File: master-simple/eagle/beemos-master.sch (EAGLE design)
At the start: 62 parts, among them CON1 BAT, CON2 JACK_DC_BARREL, CON3 SPI, IC1 32U4, IC2 MCP73831T, IC3 MCP1703CB, IC4 DMP1045U, IC5 MS5637WIDE, J1 RJ123.3, J10 RJ12STRAIGHT-I2C, J2 RJ123.3, J3 RJ123.3, J4 RJ123.3, J5 RJ123.3, J6 RJ123.3, J8 RJ123.3, J9 RJ12STRAIGHT-I2C, X1 8MHz, X2 MINI-USB, X3 1503_09

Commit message: Reorganized components, placement. Cleanup of temporary files
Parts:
- removed 100K: 100k, rcl:R-EU_R0805
- removed 868MHZ: (no value), sma_end_launch:SMACONNECTOR_EDGE_UFL
- removed C12, C13: 100n, rcl:C-EUC0805
- removed IC5: MS5637WIDE, MS5637:MS5637WIDE
- removed J10, J9: RJ12STRAIGHT-I2C, lpatiny:RJ12STRAIGHT-I2C
- removed J5, J6, J8: RJ123.3, lpatiny:RJ123.3
- removed SJ4, SJ5: JUMPER-PAD-2-NC_BY_TRACE, SparkFun-Passives:JUMPER-PAD-2-NC_BY_TRACE
- removed U$7: RN2483_SIMPLE, Octanis1_bioreactorPort:RN2483_SIMPLE
- added R13: 100, rcl:R-EU_R0805
- added R7: 1K, rcl:R-EU_R0805
- added R8, RT3: 4.7k, resistor:R-EU_R0805
- added U2: (no value), RHT03_DHT-22_AM2302:RHT03_DHT-22_AM2302
- added X4: 1503_09, con-lumberg:1503_09
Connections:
- removed net ANGND: 868MHZ.GND1, 868MHZ.GND2, 868MHZ.GND3, 868MHZ.GND4, C12.2, C13.2, SJ4.2, SJ5.2, U$7.P$1, U$7.P$21, U$7.P$26, U$7.P$27, U$7.P$33
- removed net ANT868: 868MHZ.ANT, U$7.P$23
- removed net N$27: J8.1
- removed net N$28: J8.2
- removed net N$29: J8.3
- removed net N$30: J8.4
- removed net N$31: J8.5
- removed net N$32: J8.6
- removed net N$33: J9.1
- removed net N$36: J9.4
- removed net N$37: J9.5
- removed net N$40: J9.6
- removed net N$44: J10.1
- removed net N$47: J10.4
- removed net N$48: J10.5
- removed net N$49: J10.6
- new net A8: R7.1
- new net N$2: R7.2, RT3.2, X4.2
- new net N$4: R13.1, RT3.1, X4.1
- net 3.3V: now also R13.2; no longer 100K.1, C12.1, C13.1, J5.5, J6.5, U$7.P$12
- net A2: no longer 100K.2, U$7.P$32
- net A4: no longer J5.3
- net D11: no longer J5.2
- net D12: no longer J6.3
- net D6: now also R8.1, U2.DATA; no longer J2.2
- net D7: now also R8.2, U2.VDD
- net D8: now also J2.2; no longer J6.2
- net GND: now also U2.GND, X4.3; no longer J5.4, J6.4, SJ4.1, SJ5.1
- net RX: no longer U$7.P$6
- net SCL: no longer J10.2, J5.1, J6.1, J9.2
- net SDA: no longer J10.3, J5.6, J6.6, J9.3
- net TX: no longer U$7.P$7
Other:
- note added: "I2C"
- note removed: "Barometric pressure"
- note removed: "LoRa RN2483"
- note removed: "RJ12 connectors"
- moved on the sheet: J1, J2, J3, J4, R10, R2, R9, RT1, RT2, X3

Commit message: Almost finished beemos master board (labels to do still)
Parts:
- removed U$6: SIM800L, SIM800L:SIM800L
- removed U$8: DS18B20, lpatiny:DS18B20SMALL
- removed U2: (no value), RHT03_DHT-22_AM2302:RHT03_DHT-22_AM2302
- added JP1: (no value), SparkFun:M06RA
- added R14, R16: 10k, rcl:R-EU_R0805
- added X5: 1503_09, con-lumberg:1503_09
- J1, J2, J3, J4: value RJ123.3 -> RJ12STRAIGHT-I2C; device lpatiny:RJ123.3 -> lpatiny:RJ12STRAIGHT-I2C
- R10: value 1K -> 100
- R8: value 4.7k -> 1K; device resistor:R-EU_R0805 -> rcl:R-EU_R0805
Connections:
- removed net A7: R9.1
- removed net A8: R7.1
- removed net D12*: R10.1
- removed net D14: R1.2, R6.2, U$1.VCC
- removed net N$15: C5.1, D1.C, D2.C, D3.A, D4.C, IC2.VDD, IC4.G, R15.2
- new net N$5: C5.1, D1.C, D2.C, D3.A, D4.C, IC2.VDD, IC4.G, R14.1, R15.2
- new net N$7: R16.2
- new net N$8: R8.2, RT2.2, X5.2
- net 3.3V: now also R10.2; no longer J1.5, J2.5, J3.5, J4.5, RT2.1, U$6.RST, U$8.VDD
- net A0: no longer J1.3
- net A1: no longer J2.3
- net A2: no longer J3.3
- net A3: no longer J4.3
- net A5: now also R14.2, R16.1
- net D10: now also R9.1; no longer J4.2
- net D11: now also R7.1
- net D5: no longer J1.2
- net D6: now also JP1.3; no longer R8.1, U2.DATA
- net D7: now also R8.1; no longer R8.2, U2.VDD
- net D8: no longer J2.2
- net D9: now also U$1.VCC; no longer J3.2
- net GND: now also J1.6, J2.6, J3.6, J4.6, JP1.6, X5.3; no longer U$6.GND, U$8.GND, U2.GND
- net N$9: now also R10.1, RT2.1, X5.1; no longer R10.2, RT2.2, U$8.DQ
- net RX: now also JP1.5; no longer U$6.TXD
- net SCL: now also J1.2, J2.2, J3.2, J4.2; no longer J1.1, J2.1, J3.1, J4.1
- net SDA: now also J1.3, J2.3, J3.3, J4.3; no longer J1.6, J2.6, J3.6, J4.6
- net TX: now also JP1.4; no longer U$6.RXD
- net VBAT1: now also JP1.2; no longer U$6.VDD
- net VDD: now also J1.5, J2.5, J3.5, J4.5, R1.2, R6.2
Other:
- moved on the sheet: J1, J2, J3, J4, R10, R13, R7, R8, RT2, RT3, X4

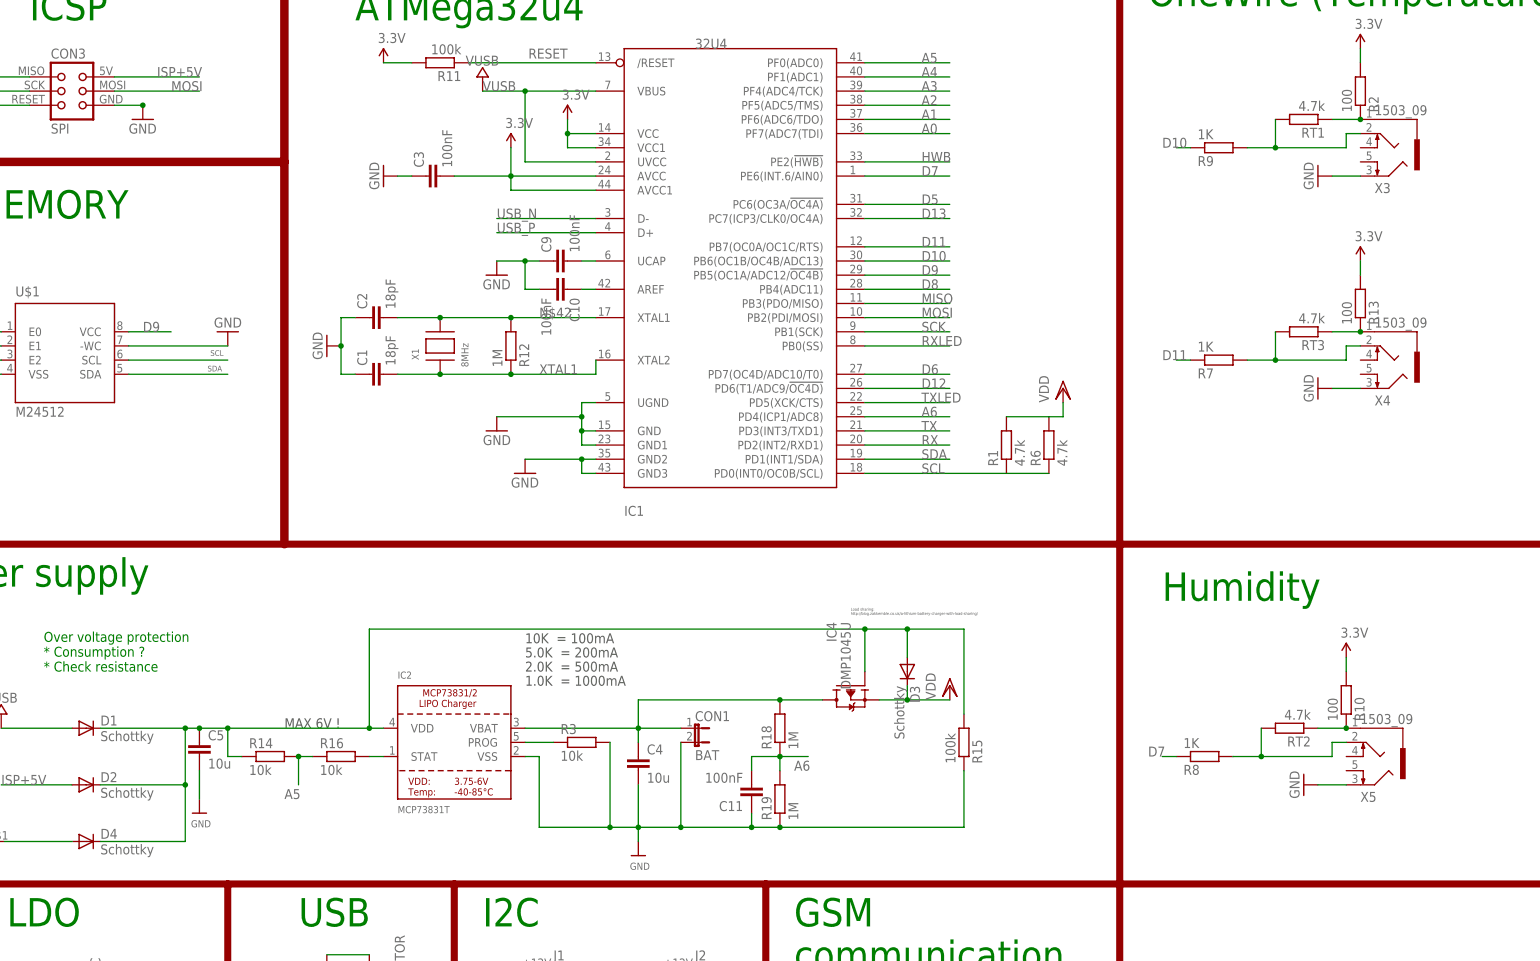
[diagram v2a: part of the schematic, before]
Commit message: Repositioned labels on the board layout
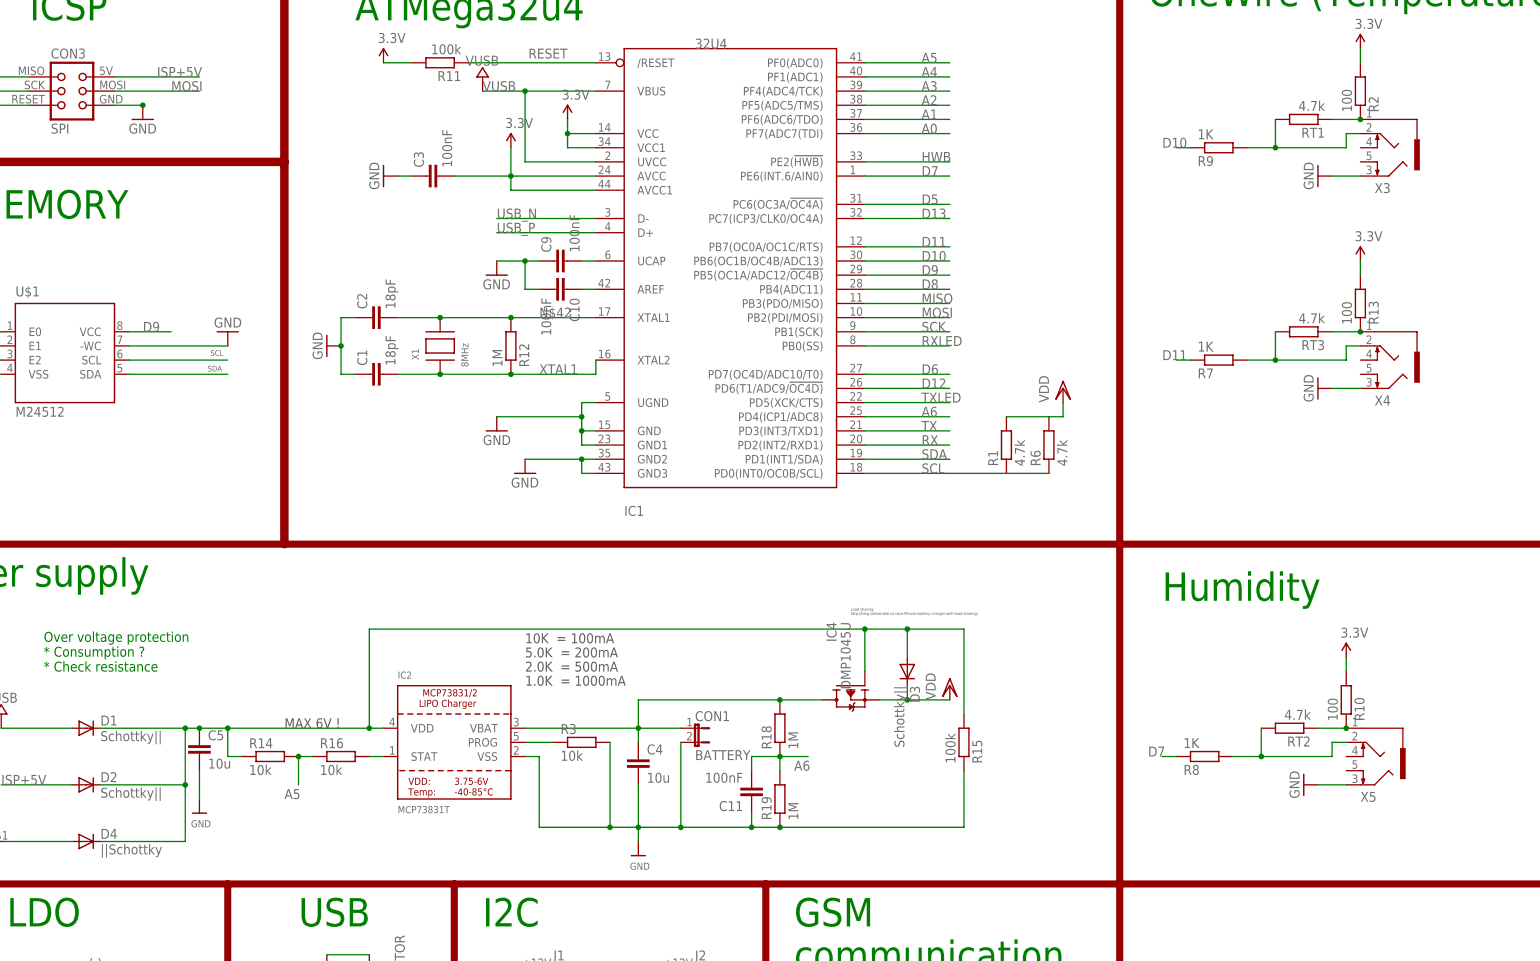
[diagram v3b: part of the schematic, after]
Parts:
- CON1: value BAT -> BATTERY
- D1, D2, D3: value Schottky -> Schottky||
- D4: value Schottky -> ||Schottky
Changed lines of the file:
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@@
 <?xml version="1.0" encoding="utf-8"?>
 <!DOCTYPE eagle SYSTEM "eagle.dtd">
-<eagle version="8.7.1">
+<eagle version="9.0.0">
 <drawing>
 <settings>
@@
 <attribute name="MPN" value="RC1206FR-07100KL"/>
 </part>
-<part name="D3" library="diode" library_urn="urn:adsk.eagle:library:210" deviceset="MBR0520LT" device="" package3d_urn="urn:adsk.eagle:package:43420/1" value="Schottky">
+<part name="D3" library="diode" library_urn="urn:adsk.eagle:library:210" deviceset="MBR0520LT" device="" package3d_urn="urn:adsk.eagle:package:43420/1" value="Schottky||">
 <attribute name="LCSC" value="C82544"/>
 <attribute name="MPN" value="621-1N5819HW-F"/>
@@
 <part name="SUPPLY4" library="supply1" library_urn="urn:adsk.eagle:library:371" deviceset="VDD" device=""/>
 <part name="U$2" library="MyPOW" deviceset="VUSB" device=""/>
-<part name="D1" library="diode" library_urn="urn:adsk.eagle:library:210" deviceset="MBR0520LT" device="" package3d_urn="urn:adsk.eagle:package:43420/1" value="Schottky">
+<part name="D1" library="diode" library_urn="urn:adsk.eagle:library:210" deviceset="MBR0520LT" device="" package3d_urn="urn:adsk.eagle:package:43420/1" value="Schottky||">
 <attribute name="LCSC" value="C82544"/>
 <attribute name="MPN" value="621-1N5819HW-F"/>
 </part>
-<part name="D2" library="diode" library_urn="urn:adsk.eagle:library:210" deviceset="MBR0520LT" device="" package3d_urn="urn:adsk.eagle:package:43420/1" value="Schottky">
+<part name="D2" library="diode" library_urn="urn:adsk.eagle:library:210" deviceset="MBR0520LT" device="" package3d_urn="urn:adsk.eagle:package:43420/1" value="Schottky||">
 <attribute name="LCSC" value="C82544"/>
 <attribute name="MPN" value="621-1N5819HW-F"/>
@@
 <attribute name="MPN" value="RC1206FR-07100KL"/>
 </part>
-<part name="CON1" library="jumper" library_urn="urn:adsk.eagle:library:252" deviceset="JP1E" device="" package3d_urn="urn:adsk.eagle:package:15455/1" value="BAT"/>
+<part name="CON1" library="jumper" library_urn="urn:adsk.eagle:library:252" deviceset="JP1E" device="" package3d_urn="urn:adsk.eagle:package:15455/1" value="BATTERY"/>
 <part name="R18" library="rcl" deviceset="R-EU_" device="R0805" value="1M">
 <attribute name="ELECROW" value="C17514"/>
@@
 <part name="J4" library="lpatiny" deviceset="RJ12" device="STRAIGHT-I2C" value="RJ12STRAIGHT-I2C"/>
 <part name="CON2" library="lpatiny" deviceset="JACK_DC_BARREL" device=""/>
-<part name="D4" library="diode" library_urn="urn:adsk.eagle:library:210" deviceset="MBR0520LT" device="" package3d_urn="urn:adsk.eagle:package:43420/1" value="Schottky">
+<part name="D4" library="diode" library_urn="urn:adsk.eagle:library:210" deviceset="MBR0520LT" device="" package3d_urn="urn:adsk.eagle:package:43420/1" value="||Schottky">
 <attribute name="LCSC" value="C82544"/>
 <attribute name="MPN" value="621-1N5819HW-F"/>
@@
 <part name="R9" library="rcl" deviceset="R-EU_" device="R0805" value="1K"/>
 <part name="P+37" library="SparkFun" deviceset="3.3V" device=""/>
-<part name="X3" library="con-lumberg" deviceset="1503_09" device=""/>
+<part name="X3" library="con-lumberg" deviceset="1503_09" device="" value=""/>
 <part name="R2" library="rcl" deviceset="R-EU_" device="R0805" value="100"/>
 <part name="GND1" library="supply1" deviceset="GND" device=""/>
@@
 <part name="R7" library="rcl" deviceset="R-EU_" device="R0805" value="1K"/>
 <part name="P+5" library="SparkFun" deviceset="3.3V" device=""/>
-<part name="X4" library="con-lumberg" deviceset="1503_09" device=""/>
+<part name="X4" library="con-lumberg" deviceset="1503_09" device="" value=""/>
 <part name="R13" library="rcl" deviceset="R-EU_" device="R0805" value="100"/>
 <part name="R14" library="rcl" deviceset="R-EU_" device="R0805" value="10k">
@@
 <part name="R8" library="rcl" deviceset="R-EU_" device="R0805" value="1K"/>
 <part name="P+6" library="SparkFun" deviceset="3.3V" device=""/>
-<part name="X5" library="con-lumberg" deviceset="1503_09" device=""/>
+<part name="X5" library="con-lumberg" deviceset="1503_09" device="" value=""/>
 <part name="R10" library="rcl" deviceset="R-EU_" device="R0805" value="100"/>
 <part name="JP1" library="SparkFun" deviceset="M06" device="RA"/>
